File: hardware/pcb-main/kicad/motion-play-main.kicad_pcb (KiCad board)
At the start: 4 copper layers, 87.8 x 40 mm, 83 parts, among them IC1 SN74AHCT125PWR, J3 LED_Strip, J4 Conn_01x05, J5 Conn_01x05, J6 Conn_01x05, J7 TYPE-C-31-M-12, J8 JST_PH_2pin, Q2 PMOS, U1 AP2112K-3.3TRG1, U2 T-Display-S3, U4 TCA9548APWR, U5 BQ24195RGER, U6 TPS61088RHLR, U7 INA219AIDCNR

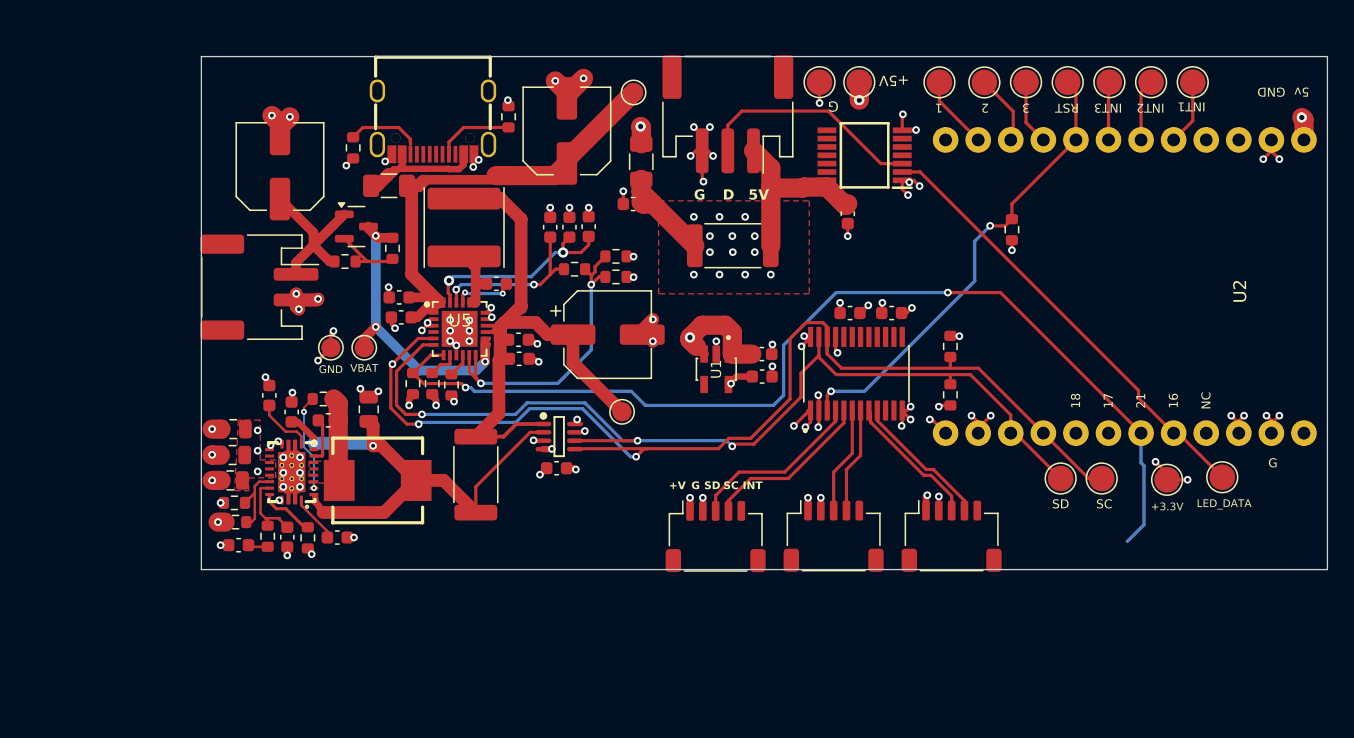
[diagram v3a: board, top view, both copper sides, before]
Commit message: Add routing verification tool and complete board routing
Build verify-routing.py that programmatically checks the routed PCB against
ROUTING_GUIDE.md specs using kiutils. Runs 20 checks across 7 categories:
trace widths, zone existence, critical path connectivity, I2C length matching,
I2C isolation from switching nodes, INA219 Kelvin sense paths, and FB/COMP
routing side verification. Produces Markdown + JSON reports.

Initial run: 16 PASS, 4 FAIL (trace widths on 15 Default-class segments,
missing B.Cu GND zone, I2C main trunk 11mm length mismatch, missing VSYS
Kelvin sense path from R44.1→U7.1).

Also includes: regenerated pcb-layout-context.json with pad data, ERC/DRC
reports, routing-verification initiative docs, and latest PCB routing state.

Made-with: Cursor
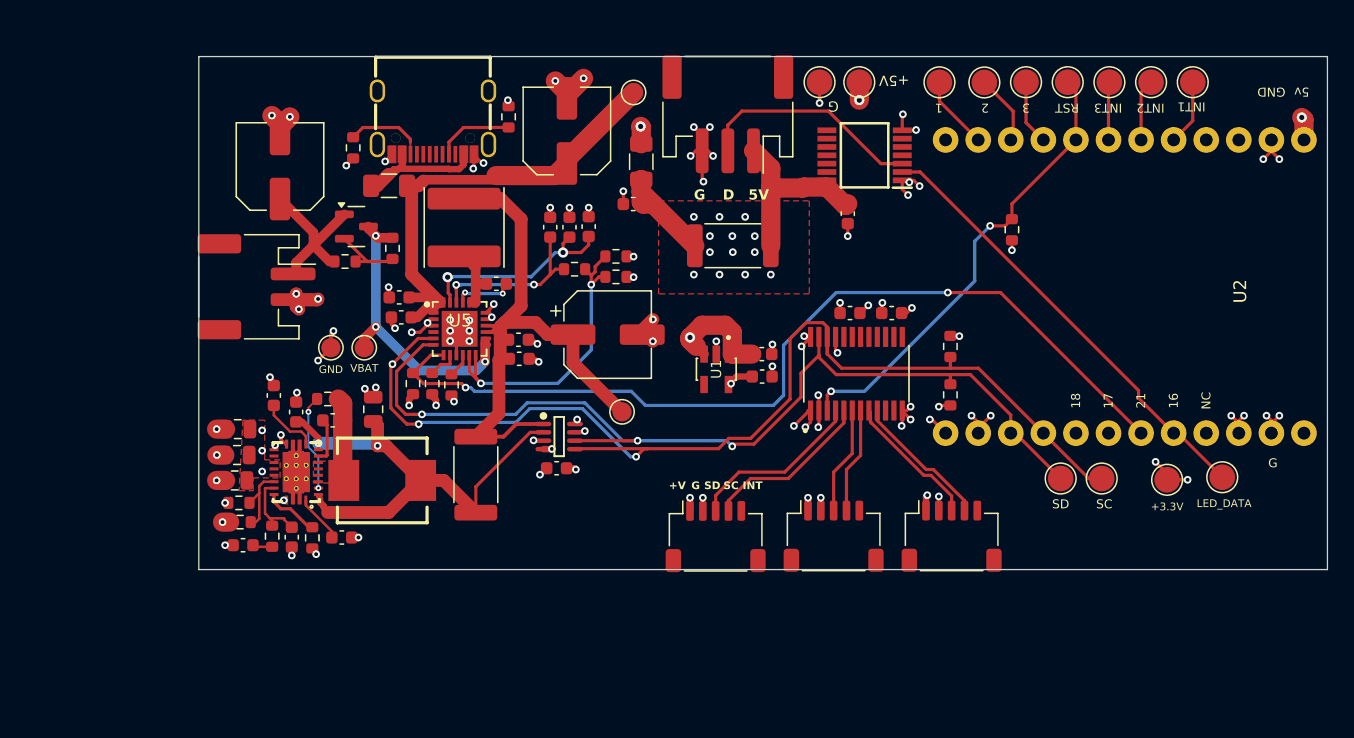
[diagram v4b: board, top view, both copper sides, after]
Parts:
- moved C33 0.35 mm to (87.2, 138.5)
- moved C35 0.35 mm to (79.0, 130.1)
- moved C38 0.35 mm to (79.5, 139.1)
- moved U6 0.35 mm to (83.6, 133.4)
- moved C31 0.35 mm to (83.6, 128.7)
- moved C32 0.35 mm to (86.4, 129.4)
- moved C34 0.35 mm to (79.0, 132.1)
- moved C36 0.35 mm to (78.8, 134.1)
- moved C37 0.35 mm to (81.8, 127.4)
- moved C39 0.35 mm to (83.2, 138.5)
- moved C41 0.35 mm to (89.6, 128.5)
- moved L2 0.35 mm to (90.3, 134.1)
- moved R39 0.35 mm to (79.2, 137.3)
- moved R40 0.35 mm to (79.1, 135.8)
- moved R41 0.35 mm to (86.0, 127.7)
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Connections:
- J4 pad 5: /INT1 -> unconnected-(J4-Pin_5-Pad5)
- J5 pad 5: /INT2 -> unconnected-(J5-Pin_5-Pad5)
- J6 pad 5: /INT3 -> unconnected-(J6-Pin_5-Pad5)
- U6 pad : (no net) -> GND
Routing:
- net /Power Management/CHRG_INT: track 80.4 -> 71.4 mm
- net GND: track 94.0 -> 96.2 mm, vias 113 -> 106
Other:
- board size 87.8 x 40 mm -> 88 x 40 mm

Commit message: Fix routing verification, add B.Cu GND zone, install power switch footprint
Verification script improvements:
- Fix Kelvin sense check to use threshold (< half power width) instead of
  exact 0.25mm match, correctly identifying 0.30mm dedicated sense traces
- Fix connectivity graph to use distance-based merging instead of grid
  quantization, resolving false disconnection on Protected_VBUS path
- Downgrade minor trace width deviations (<=0.1mm) to warnings
- Exempt GND from trace width checks (uses planes, widths vary by design)

Board updates:
- Add B.Cu GND zone (bottom ground fill)
- Tweak BOOST_FSW/VCC/SS/CC2 trace widths, I2C trunk length balancing

Verification now passes: 19 PASS, 0 FAIL, 1 WARNING.

Also install JLC-MCP library footprints for SS12D11-WG12 power switch
(BXCONN, 3A SPDT, right-angle, C49563384) in preparation for battery
on/off switch addition.

Made-with: Cursor
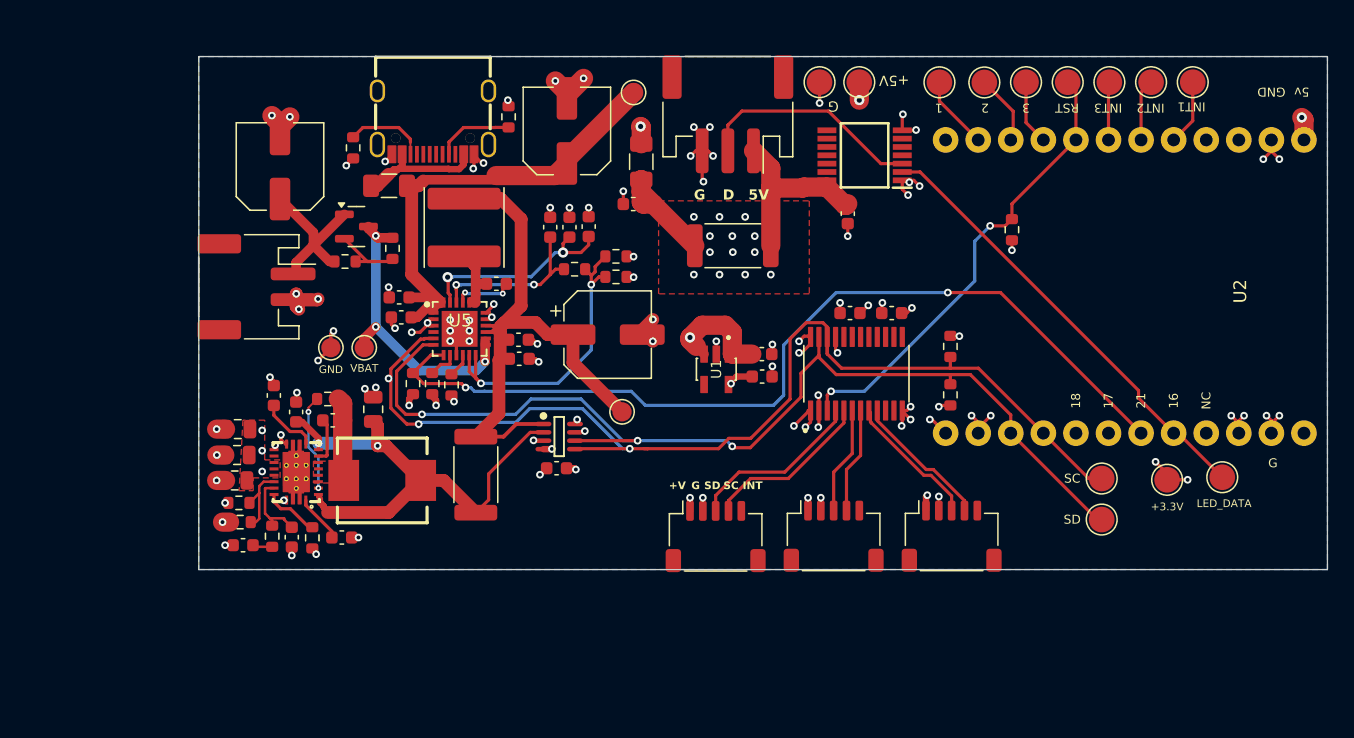
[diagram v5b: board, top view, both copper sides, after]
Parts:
- moved TPIO43 4.53 mm to (146.4, 137.1)
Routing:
- net /I2C_SDA: track 76.8 -> 82.0 mm
- net /I2C_SCL: track 88.1 -> 86.6 mm
- net +3.3V: track 17.8 -> 19.0 mm
- added copper zone on B.Cu, net GND

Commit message: Update LCSC part numbers for JLCPCB assembly and finalize manufacturing files
Resolve JLCPCB assembly stock issues by substituting unavailable parts:
- C2836440 → C7469958 (47µF FOSAN, D6.3×5.4mm, Economic PCBA compatible)
- C59461 → C109314 (22µF YAGEO 0805, fixes package mismatch)
- C14663 restored (100nF, restocked in JLCPCB assembly)
- J4-J6, Q2, R27 LCSC corrections from prior commit synced to PCB

Re-extracted circuit-context.json and pcb-layout-context.json.
Added cursor rule documenting hardware file conventions.
Cleaned up stale KiCad backup files.

Order placed on JLCPCB 2026-03-16.

Made-with: Cursor
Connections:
- U6 pad : GND -> (no net)
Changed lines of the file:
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@@
 			(layers "*.Cu" "*.Paste" "*.Mask")
 			(remove_unused_layers no)
-			(net 10 "GND")
 		)
 		(pad "" thru_hole circle
@@
 			(layers "*.Cu" "*.Paste" "*.Mask")
 			(remove_unused_layers no)
-			(net 10 "GND")
 		)
 		(pad "" thru_hole circle
@@
 			(layers "*.Cu" "*.Paste" "*.Mask")
 			(remove_unused_layers no)
-			(net 10 "GND")
 		)
 		(pad "" thru_hole circle
@@
 			(layers "*.Cu" "*.Paste" "*.Mask")
 			(remove_unused_layers no)
-			(net 10 "GND")
 		)
 		(pad "" thru_hole circle
@@
 			(layers "*.Cu" "*.Paste" "*.Mask")
 			(remove_unused_layers no)
-			(net 10 "GND")
 		)
 		(pad "" thru_hole circle
@@
 			(layers "*.Cu" "*.Paste" "*.Mask")
 			(remove_unused_layers no)
-			(net 10 "GND")
 		)
 		(pad "" thru_hole circle
@@
 			(layers "*.Cu" "*.Paste" "*.Mask")
 			(remove_unused_layers no)
-			(net 10 "GND")
 		)
 		(pad "" thru_hole circle
@@
 			(layers "*.Cu" "*.Paste" "*.Mask")
 			(remove_unused_layers no)
-			(net 10 "GND")
 		)
 		(pad "1" smd rect
@@
 			)
 		)
-		(property "LCSC Part" "C59461"
+		(property "LCSC Part" "C109314"
 			(at 0 0 180)
 			(unlocked yes)
@@
 			)
 		)
-		(property "LCSC Part" "C14663"
+		(property "LCSC Part" "C92490"
 			(at 0 0 180)
 			(unlocked yes)
@@
 			)
 		)
-		(property "LCSC Part" "C59461"
+		(property "LCSC Part" "C109314"
 			(at 0 0 180)
 			(unlocked yes)
@@
 			)
 		)
-		(property "LCSC Part" "C14663"
+		(property "LCSC Part" "C92490"
 			(at 0 0 0)
 			(unlocked yes)
@@
 			)
 		)
-		(property "LCSC Part No" "C14663"
+		(property "LCSC Part No" "C92490"
 			(at 0 0 180)
 			(unlocked yes)
@@
 			)
 		)
-		(property "LCSC Part" "C14663"
+		(property "LCSC Part" "C92490"
 			(at 0 0 180)
 			(unlocked yes)
@@
 			)
 		)
-		(property "LCSC Part" "C14663"
+		(property "LCSC Part" "C92490"
 			(at 0 0 90)
 			(unlocked yes)
@@
 			)
 		)
-		(property "LCSC Part No" "C14663"
+		(property "LCSC Part No" "C92490"
 			(at 0 0 0)
 			(unlocked yes)
@@
 			)
 		)
-		(property "LCSC Part" "C14663"
+		(property "LCSC Part" "C92490"
 			(at 0 0 0)
 			(unlocked yes)
@@
 			)
 		)
-		(property "LCSC Part" "C2836440"
+		(property "LCSC Part" "C3344"
 			(at 0 0 90)
 			(unlocked yes)
@@
 			)
 		)
-		(property "LCSC Part" "C59461"
+		(property "LCSC Part" "C109314"
 			(at 0 0 180)
 			(unlocked yes)
@@
 			)
 		)
-		(property "LCSC Part" "C2836440"
+		(property "LCSC Part" "C3344"
 			(at 0 0 90)
 			(unlocked yes)
@@
 		(polygon
 			(pts
-				(xy 163.75 101) (xy 66.65 101) (xy 66.65 141) (xy 163.75 141)
+				(xy 163.75 101) (xy 76.05 101) (xy 76.05 141) (xy 163.75 141)
 			)
 		)

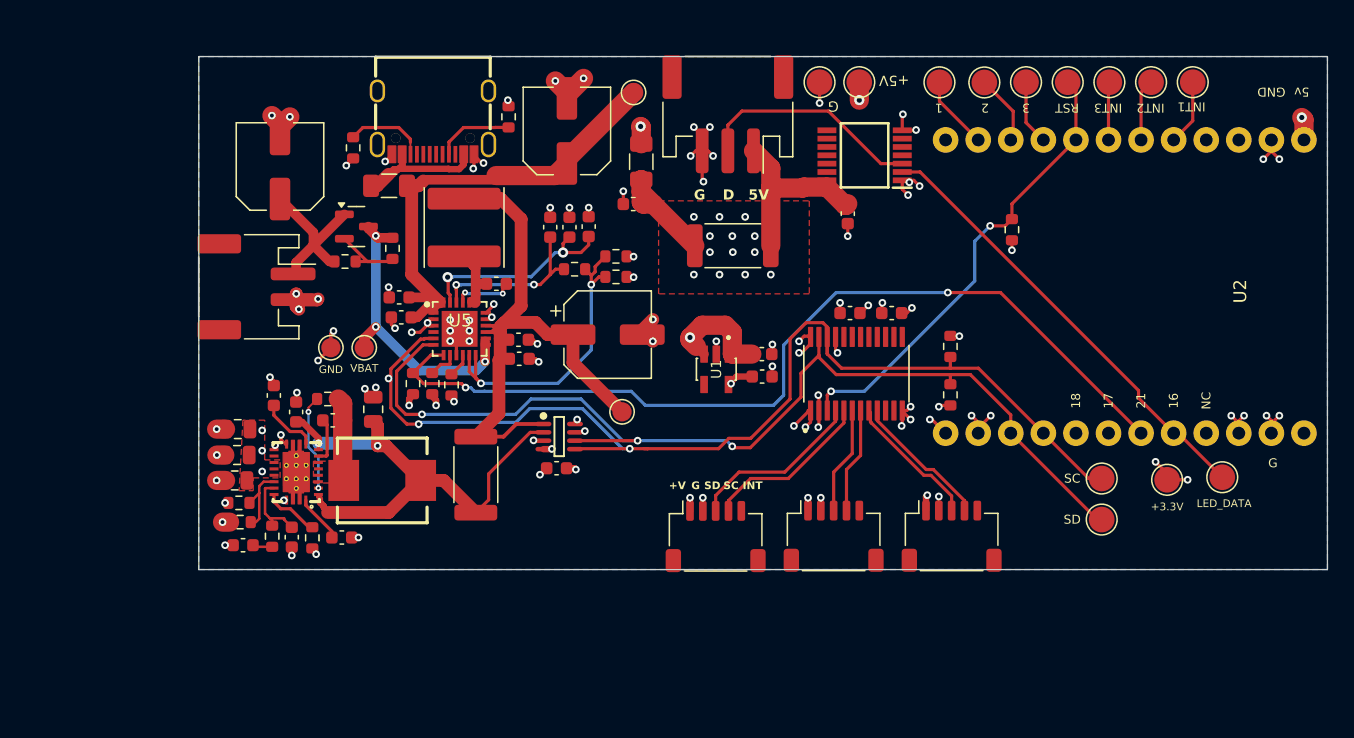
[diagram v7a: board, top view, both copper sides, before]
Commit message: Phase 2 PCB layout: component placement, footprint libs, routing/placement guides
All 20 new ESP32 integration components placed on the board. Added
missing JLC-MCP footprints to project library. Created placement and
routing guide documents. Configured USB net class (0.1mm clearance),
antenna keepout zone, and U8 thermal copper pour.

Made-with: Cursor
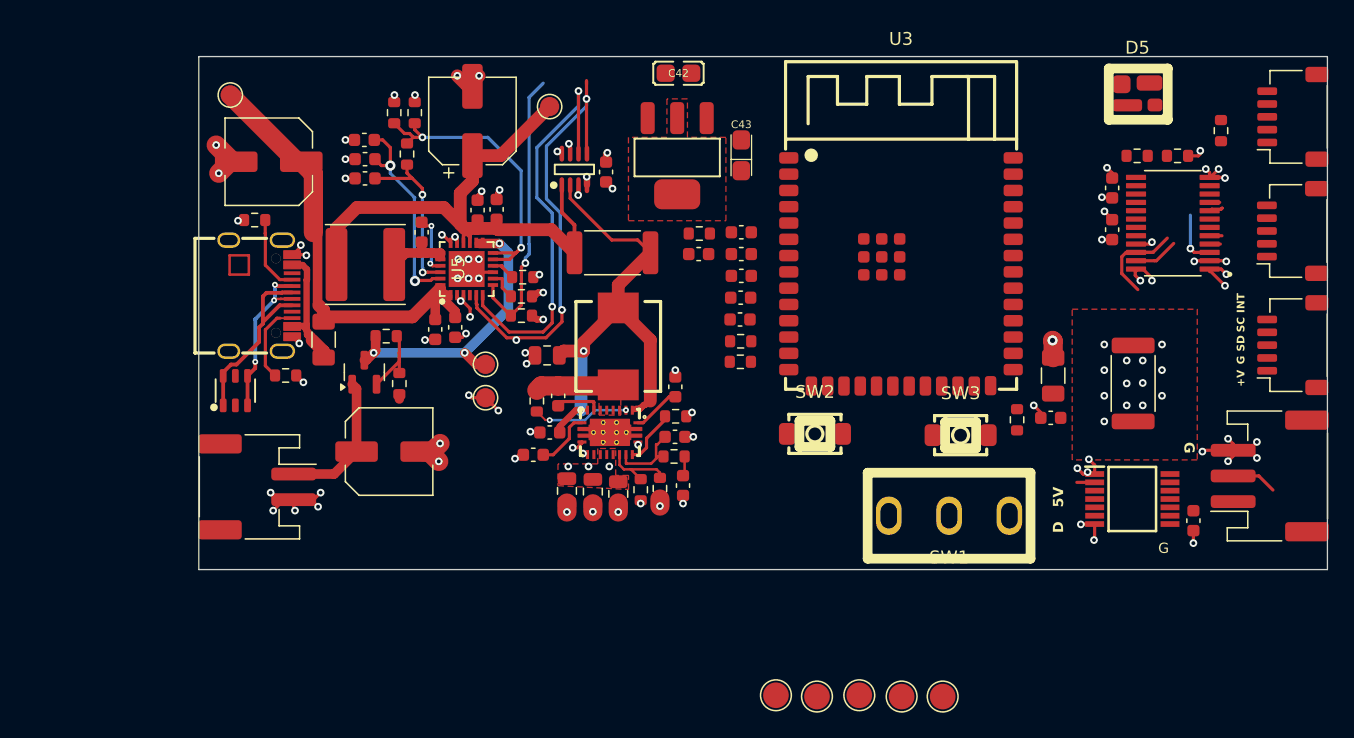
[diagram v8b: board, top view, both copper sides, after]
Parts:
- removed C1: 1µF, Capacitor_SMD:C_0603_1608Metric
- removed C2: 2.2µF, Capacitor_SMD:C_0603_1608Metric
- removed TPIO1, TPIO11, TPIO12, TPIO13, TPIO2, TPIO3, TP_3V1, TP_5V1, TP_GND1: TestPoint, TestPoint:TestPoint_Pad_D2.0mm
- removed U1: AP2112K-3.3TRG1, motion-play-footprints:SOT95P285X140-5N
- removed U2: T-Display-S3, motion-play-footprints:T-Display-S3
- added C42: 22uF, JLC-MCP:C0805, F.Cu at (113.4, 102.3)
- added C43: 22uF 6.3V Tant, JLC-MCP:CASE-A_3216, F.Cu at (118.3, 108.7)
- added C50: 1µF, Capacitor_SMD:C_0603_1608Metric, F.Cu at (115.0, 116.4)
- added C51: 10µF, Capacitor_SMD:C_0603_1608Metric, F.Cu at (118.3, 114.7)
- added C52: 100nF, Capacitor_SMD:C_0603_1608Metric, F.Cu at (118.3, 116.4)
- added C53: 100nF, Capacitor_SMD:C_0603_1608Metric, F.Cu at (118.3, 118.1)
- added C54: 100nF, Capacitor_SMD:C_0603_1608Metric, F.Cu at (118.2, 119.8)
- added C55: 1µF, Capacitor_SMD:C_0603_1608Metric, F.Cu at (118.2, 121.5)
- added D5: WS2812B-MINI, JLC-MCP:LED-SMD_4P-L3.5-W3.5-TL_WS2812B-1, F.Cu at (149.2, 103.9)
- added R50: 10kΩ, Resistor_SMD:R_0603_1608Metric, F.Cu at (115.0, 114.8)
- added R51: 10kΩ, Resistor_SMD:R_0603_1608Metric, F.Cu at (139.8, 129.3)
- added R52: 22Ω, Resistor_SMD:R_0603_1608Metric, F.Cu at (118.2, 123.2)
- added R53: 22Ω, Resistor_SMD:R_0603_1608Metric, F.Cu at (118.2, 124.8)
- added SW1: SS-12D10L5, JLC-MCP:SW-TH_SS-12D10L5, F.Cu at (134.5, 136.8)
- added SW2: RESET, JLC-MCP:KEY-SMD_L4.0-W3.0-LS4.9-1, F.Cu at (124.0, 130.4)
- added SW3: BOOT, JLC-MCP:KEY-SMD_L4.0-W3.0-LS4.9-1, F.Cu at (135.4, 130.5)
- added TPIO21: TestPoint, TestPoint:TestPoint_Pad_D2.0mm, F.Cu at (121.0, 150.8)
- added U3: ESP32-S3-WROOM-1-N16R8, JLC-MCP:WIRELM-SMD_ESP32-S3-WROOM-1, F.Cu at (130.8, 117.8)
- added U8: AMS1117-3.3, JLC-MCP:SOT-223-3_L6.5-W3.4-P2.30-LS7.0-BR, F.Cu at (113.3, 108.7)
- added U9: USBLC6-2SC6, JLC-MCP:SOT-23-6_L2.9-W1.6-P0.95-LS2.8-BL, F.Cu at (78.8, 127.0)
- moved TPIO10 51.7 mm to (124.2, 150.9)
- moved J3 50.8 mm to (159.5, 133.7), turned to 90 degrees
- moved J4 47.4 mm to (161.3, 123.5), turned to 90 degrees
- moved J5 43.0 mm to (161.3, 114.6), turned to 90 degrees
- moved J6 42.2 mm to (161.3, 105.7), turned to 90 degrees
- moved C7 36.6 mm to (142.4, 129.2)
- moved F1 36.2 mm to (142.6, 125.9)
- moved C8 36.0 mm to (153.6, 137.2)
- moved C38 34.6 mm to (113.8, 134.4), turned to -90 degrees
- moved IC1 34.0 mm to (148.8, 135.5), turned to 0 degrees
- moved R27 33.0 mm to (148.8, 126.5), turned to -90 degrees
- moved R39 32.8 mm to (112.0, 134.7), turned to 90 degrees
- moved R43 31.9 mm to (113.1, 132.2), turned to 0 degrees
- moved TP3 31.4 mm to (78.5, 104.0), turned to 90 degrees
- moved R40 31.3 mm to (110.5, 134.8), turned to -90 degrees
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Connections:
- net /LED Controller/DATA_IN renamed /LED_DATA
- net /Power Management/CHRG_INT renamed /CHRG_INT
- net /TCA9548A_Subsystem/TCA_RESET renamed /TCA_RESET
- J7 pad A6: unconnected-(J7-DP1-PadA6) -> /USB_DP
- J7 pad A7: unconnected-(J7-DN1-PadA7) -> /USB_DN
- J7 pad B6: unconnected-(J7-DP2-PadB6) -> /USB_DP
- J7 pad B7: unconnected-(J7-DN2-PadB7) -> /USB_DN
- R44 pad 1: /Power Management/VSYS -> /Power Management/VSYS_SW
- U7 pad 1: /Power Management/VSYS -> /Power Management/VSYS_SW
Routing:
- net /CHRG_INT: track 71.4 -> 22.1 mm, vias 2 -> 1
- net /I2C_SDA: track 82.0 -> 35.7 mm, vias 3 -> 2
- net /I2C_SCL: track 86.6 -> 43.6 mm
- net /LED_DATA: track 35.2 -> 1.39 mm
- net /TCA_RESET: track 36.3 -> 4.22 mm, vias 2 -> 1
- net GND: track 96.2 -> 80.6 mm, vias 106 -> 92
- net /USB_DP: track 0.00 -> 15.4 mm
- net /LED Controller/+5V_TO_LEDS: track 14.6 -> 0.00 mm
- net /LED Controller/DATA_TO_LEDS: track 17.8 -> 3.56 mm
- net /USB_DN: track 0.00 -> 13.2 mm, vias 0 -> 3
- net /TCA9548A_Subsystem/CH0_SDA: track 13.8 -> 0.84 mm
- net /TCA9548A_Subsystem/CH0_SCL: track 13.3 -> 0.96 mm
- net +5V: track 14.0 -> 1.92 mm, vias 8 -> 5
- net /TCA9548A_Subsystem/CH2_SCL: track 10.9 -> 0.78 mm
- net +3.3V: track 19.0 -> 9.14 mm, vias 17 -> 9
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- added copper zone on F.Cu, net +3.3V
- removed copper zone on B.Cu, net GND
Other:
- board text removed: "+5V"
- board text removed: "1"
- board text removed: "LED_DATA"
